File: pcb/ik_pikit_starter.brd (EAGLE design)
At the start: 51.8 x 21.6 mm, 30 parts, among them U1 QRE1113, U2 MCP9700SMD

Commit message: adding values
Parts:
- C1, C2: value (none) -> 0.1uF
- LED1, LED2, LED3, LED4, LED5, LED6: value (none) -> BLUE
- R1: value (none) -> 100
- R10, R11, R3: value (none) -> 10K
- R2: value (none) -> 220
- R4, R5, R6, R7, R8, R9: value (none) -> 1K
- moved C1 0.52 mm to (45.5, 12.1), turned to 0 degrees
- moved C2 0.52 mm to (49.0, 12.1)
- renumbered U$1 to U3
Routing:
- net 3V3: track 46.4 -> 47.0 mm
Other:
- board text added: "ADC (i2c)"
- board text added: "CH2:Distance"
- board text removed: "I2C ADC"

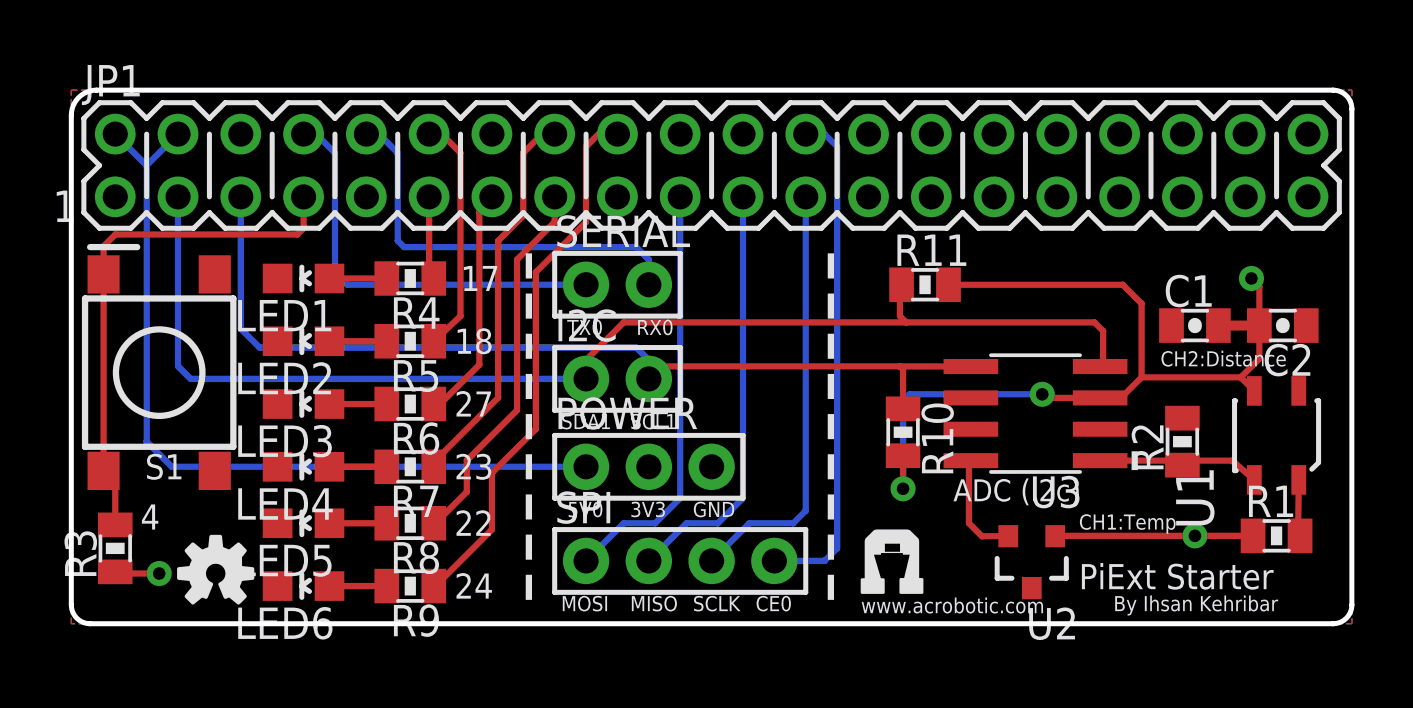
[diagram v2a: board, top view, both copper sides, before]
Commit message: fixed silkscreen
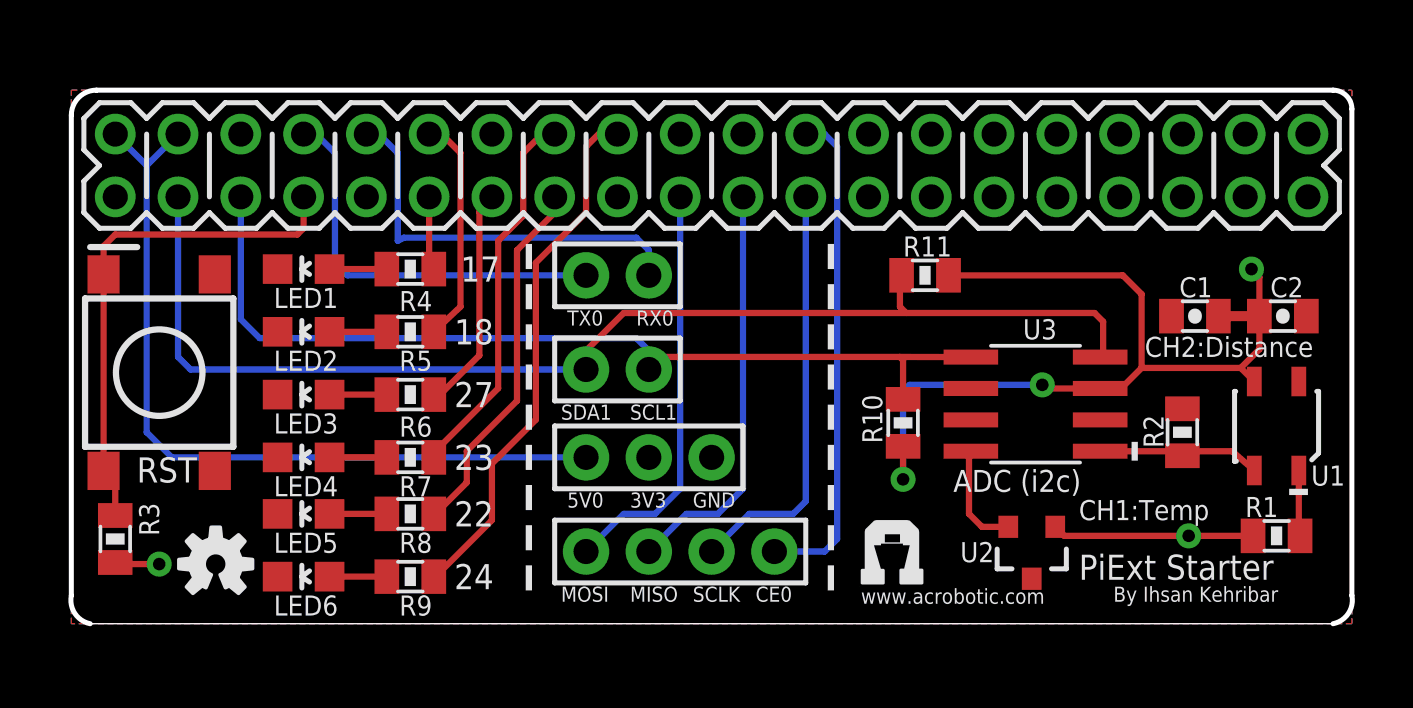
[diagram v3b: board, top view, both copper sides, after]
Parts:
- moved C1 0.38 mm to (45.5, 12.4)
- moved C2 0.38 mm to (49.0, 12.4)
- moved I2C 0.38 mm to (22.1, 10.3)
- moved LED1 0.38 mm to (9.40, 14.4)
- moved LED2 0.38 mm to (9.40, 11.8)
- moved LED3 0.38 mm to (9.40, 9.27)
- moved LED4 0.38 mm to (9.40, 6.73)
- moved LED5 0.38 mm to (9.40, 4.45)
- moved POWER 0.38 mm to (23.4, 6.73)
- moved R10 0.38 mm to (33.7, 8.13)
- moved R11 0.38 mm to (34.5, 14.1)
- moved R2 0.38 mm to (45.0, 7.75)
- moved R4 0.38 mm to (13.7, 14.4)
- moved R5 0.38 mm to (13.7, 11.8)
- moved R6 0.38 mm to (13.7, 9.27)
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- renumbered S1 to RST
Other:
- outline, holes or cut-outs redrawn
- board text removed: "4"
